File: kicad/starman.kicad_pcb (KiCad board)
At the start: 4 copper layers, 182 x 150 mm, 204 parts, among them J1 M20-8771246, J10 Barrel_Jack_MountingPin, J2 M20-8770646, J3 M20-8771246, J4 ESW-106-44-T-S, J5 Conn_02x03_Counter_Clockwise, J6 ESW-112-44-T-S, J7 Conn_01x10, J8 ESW-112-44-T-S, J9 Conn_01x10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

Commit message: DRC corrections
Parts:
- renumbered REF** to LOGO1, REF** to LOGO2
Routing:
- net Net-(D71-Pad1): track 32.7 -> 33.4 mm
- net Net-(D59-Pad1): track 22.0 -> 22.7 mm
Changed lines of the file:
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@@
     (descr "Open Source Hardware Logo")
     (tags "Logo OSHW")
-    (attr exclude_from_pos_files exclude_from_bom)
-    (fp_text reference "REF**" (at 0 0) (layer "F.SilkS") hide
+    (attr board_only exclude_from_pos_files exclude_from_bom)
+    (fp_text reference "LOGO2" (at 0 0) (layer "F.SilkS") hide
       (effects (font (size 1 1) (thickness 0.15)))
     )
@@
     (descr "KiCad Logo")
     (tags "Logo KiCad")
-    (attr exclude_from_pos_files exclude_from_bom)
-    (fp_text reference "REF**" (at 0 -5.08) (layer "F.SilkS") hide
+    (attr board_only exclude_from_pos_files exclude_from_bom)
+    (fp_text reference "LOGO1" (at 0 -5.08) (layer "F.SilkS") hide
       (effects (font (size 1 1) (thickness 0.15)))
     )
@@
   (segment (start 167.4625 89.7625) (end 175 97.3) (width 0.15) (layer "F.Cu") (net 16))
   (segment (start 152.5 89.7625) (end 167.4625 89.7625) (width 0.15) (layer "F.Cu") (net 16))
-  (segment (start 67.5 92.0125) (end 67.5 97.499022) (width 0.15) (layer "F.Cu") (net 17))
-  (segment (start 67.5 97.499022) (end 57.699022 107.3) (width 0.15) (layer "F.Cu") (net 17))
-  (segment (start 57.699022 107.3) (end 55 107.3) (width 0.15) (layer "F.Cu") (net 17))
+  (segment (start 67.5 92.0125) (end 67.5 98.7) (width 0.15) (layer "F.Cu") (net 17))
+  (segment (start 62.3 100) (end 55 107.3) (width 0.15) (layer "F.Cu") (net 17))
+  (segment (start 67.5 98.7) (end 66.2 100) (width 0.15) (layer "F.Cu") (net 17))
+  (segment (start 66.2 100) (end 62.3 100) (width 0.15) (layer "F.Cu") (net 17))
   (segment (start 68.2125 92.725) (end 68.2125 104.0875) (width 0.15) (layer "F.Cu") (net 18))
   (segment (start 68.2125 104.0875) (end 65 107.3) (width 0.15) (layer "F.Cu") (net 18))
@@
   (segment (start 70.2125 96.909644) (end 70.2125 92.725) (width 0.15) (layer "F.Cu") (net 20))
   (segment (start 73.402856 100.1) (end 70.2125 96.909644) (width 0.15) (layer "F.Cu") (net 20))
-  (segment (start 104.486072 119.5625) (end 103.25 118.326428) (width 0.15) (layer "F.Cu") (net 21))
-  (segment (start 103.25 118.326428) (end 103.25 109.05) (width 0.15) (layer "F.Cu") (net 21))
-  (segment (start 103.25 109.05) (end 105 107.3) (width 0.15) (layer "F.Cu") (net 21))
+  (segment (start 103.1 118.176428) (end 103.1 109.2) (width 0.15) (layer "F.Cu") (net 21))
+  (segment (start 104.486072 119.5625) (end 103.1 118.176428) (width 0.15) (layer "F.Cu") (net 21))
   (segment (start 107.5 119.5625) (end 104.486072 119.5625) (width 0.15) (layer "F.Cu") (net 21))
+  (segment (start 103.1 109.2) (end 105 107.3) (width 0.15) (layer "F.Cu") (net 21))
+  (segment (start 116.9 109.2) (end 115 107.3) (width 0.15) (layer "F.Cu") (net 22))
+  (segment (start 116.9 118.099022) (end 116.9 109.2) (width 0.15) (layer "F.Cu") (net 22))
+  (segment (start 115.436522 119.5625) (end 116.9 118.099022) (width 0.15) (layer "F.Cu") (net 22))
   (segment (start 112.525 119.5625) (end 115.436522 119.5625) (width 0.15) (layer "F.Cu") (net 22))
-  (segment (start 116.474511 118.524511) (end 116.474511 108.774511) (width 0.15) (layer "F.Cu") (net 22))
-  (segment (start 115.436522 119.5625) (end 116.474511 118.524511) (width 0.15) (layer "F.Cu") (net 22))
-  (segment (start 116.474511 108.774511) (end 115 107.3) (width 0.15) (layer "F.Cu") (net 22))
   (segment (start 146.724061 100.249511) (end 142.050489 100.249511) (width 0.15) (layer "F.Cu") (net 23))
   (segment (start 149.7875 97.186072) (end 146.724061 100.249511) (width 0.15) (layer "F.Cu") (net 23))
@@
   (segment (start 69.0125 111.3125) (end 75 117.3) (width 0.15) (layer "F.Cu") (net 28))
   (segment (start 69.0125 92.725) (end 69.0125 111.3125) (width 0.15) (layer "F.Cu") (net 28))
-  (segment (start 85 117.3) (end 82.227934 117.3) (width 0.15) (layer "F.Cu") (net 29))
-  (segment (start 69.4125 104.484566) (end 69.4125 92.725) (width 0.15) (layer "F.Cu") (net 29))
-  (segment (start 82.227934 117.3) (end 69.4125 104.484566) (width 0.15) (layer "F.Cu") (net 29))
+  (segment (start 77 109.7) (end 73.3 109.7) (width 0.15) (layer "F.Cu") (net 29))
+  (segment (start 73.3 109.7) (end 69.4125 105.8125) (width 0.15) (layer "F.Cu") (net 29))
+  (segment (start 69.4125 105.8125) (end 69.4125 92.725) (width 0.15) (layer "F.Cu") (net 29))
+  (segment (start 85 117.3) (end 84.6 117.3) (width 0.15) (layer "F.Cu") (net 29))
+  (segment (start 84.6 117.3) (end 77 109.7) (width 0.15) (layer "F.Cu") (net 29))
   (segment (start 100 119.3) (end 97 119.3) (width 0.15) (layer "F.Cu") (net 30))
   (segment (start 97 119.3) (end 95 117.3) (width 0.15) (layer "F.Cu") (net 30))
@@
   (segment (start 51.775 151.4) (end 48.025 155.15) (width 0.15) (layer "F.Cu") (net 161))
   (segment (start 38.075 174.225) (end 35 177.3) (width 0.15) (layer "F.Cu") (net 161))
-  (segment (start 38.075 165.125) (end 38.075 174.375) (width 0.15) (layer "F.Cu") (net 161))
   (segment (start 42.674999 160.375001) (end 38.075 164.975) (width 0.15) (layer "F.Cu") (net 161))
   (segment (start 48.025 155.15) (end 48.025 158.7) (width 0.15) (layer "F.Cu") (net 161))
@@
   (segment (start 46.349999 160.375001) (end 42.674999 160.375001) (width 0.15) (layer "F.Cu") (net 161))
   (segment (start 48.025 158.7) (end 46.349999 160.375001) (width 0.15) (layer "F.Cu") (net 161))
+  (segment (start 38.075 165) (end 38.075 174.375) (width 0.15) (layer "F.Cu") (net 161))
   (segment (start 51.64952 161.47548) (end 51.64952 170.65048) (width 0.15) (layer "F.Cu") (net 162))
   (segment (start 59.4 158.048572) (end 57.424061 160.024511) (width 0.15) (layer "F.Cu") (net 162))
@@
   (segment (start 133.4 90) (end 133.9 89.5) (width 0.15) (layer "F.Cu") (net 169))
   (segment (start 122.5 88.9375) (end 123.5625 90) (width 0.15) (layer "F.Cu") (net 169))
-  (segment (start 104.400489 98.700489) (end 104.9 99.2) (width 0.15) (layer "F.Cu") (net 169))
   (segment (start 159 147.4875) (end 158.951489 147.438989) (width 0.15) (layer "F.Cu") (net 169))
   (segment (start 146.768928 90.9625) (end 146.668439 90.862011) (width 0.15) (layer "F.Cu") (net 169))
@@
   (segment (start 120.7625 88.9375) (end 122.5 88.9375) (width 0.15) (layer "F.Cu") (net 169))
   (segment (start 143.862011 90.862011) (end 143.1 90.1) (width 0.15) (layer "F.Cu") (net 169))
-  (segment (start 102.2 95.9) (end 103.525489 97.225489) (width 0.15) (layer "F.Cu") (net 169))
   (segment (start 109.0125 117.65) (end 109.0125 113.4875) (width 0.15) (layer "F.Cu") (net 169))
   (segment (start 120.455216 85.702691) (end 121.447309 85.702691) (width 0.15) (layer "F.Cu") (net 169))
-  (segment (start 103.724061 98.700489) (end 104.400489 98.700489) (width 0.15) (layer "F.Cu") (net 169))
+  (segment (start 104.223572 99.2) (end 104.9 99.2) (width 0.15) (layer "F.Cu") (net 169))
   (segment (start 72.525 89.2125) (end 77.1125 89.2125) (width 0.15) (layer "F.Cu") (net 169))
   (segment (start 109.0125 113.4875) (end 109.2 113.3) (width 0.15) (layer "F.Cu") (net 169))
@@
   (segment (start 120.7625 88.9375) (end 119.477226 87.652226) (width 0.15) (layer "F.Cu") (net 169))
   (segment (start 59 143) (end 59.7 142.3) (width 0.15) (layer "F.Cu") (net 169))
-  (segment (start 102 95.9) (end 102.2 95.9) (width 0.15) (layer "F.Cu") (net 169))
   (segment (start 77.1125 89.2125) (end 77.4 89.5) (width 0.15) (layer "F.Cu") (net 169))
-  (segment (start 103.525489 98.501917) (end 103.724061 98.700489) (width 0.15) (layer "F.Cu") (net 169))
+  (segment (start 103.3 98.276428) (end 104.223572 99.2) (width 0.15) (layer "F.Cu") (net 169))
+  (segment (start 103.3 97) (end 103.3 98.276428) (width 0.15) (layer "F.Cu") (net 169))
   (segment (start 123.5625 90) (end 133.4 90) (width 0.15) (layer "F.Cu") (net 169))
   (segment (start 59 147.4875) (end 59 143) (width 0.15) (layer "F.Cu") (net 169))
-  (segment (start 103.525489 97.225489) (end 103.525489 98.501917) (width 0.15) (layer "F.Cu") (net 169))
+  (segment (start 102 95.9) (end 102.2 95.9) (width 0.15) (layer "F.Cu") (net 169))
+  (segment (start 102.2 95.9) (end 103.3 97) (width 0.15) (layer "F.Cu") (net 169))
   (segment (start 119.477226 87.652226) (end 119.477226 86.680681) (width 0.15) (layer "F.Cu") (net 169))
   (segment (start 147.475 90.9625) (end 146.768928 90.9625) (width 0.15) (layer "F.Cu") (net 169))

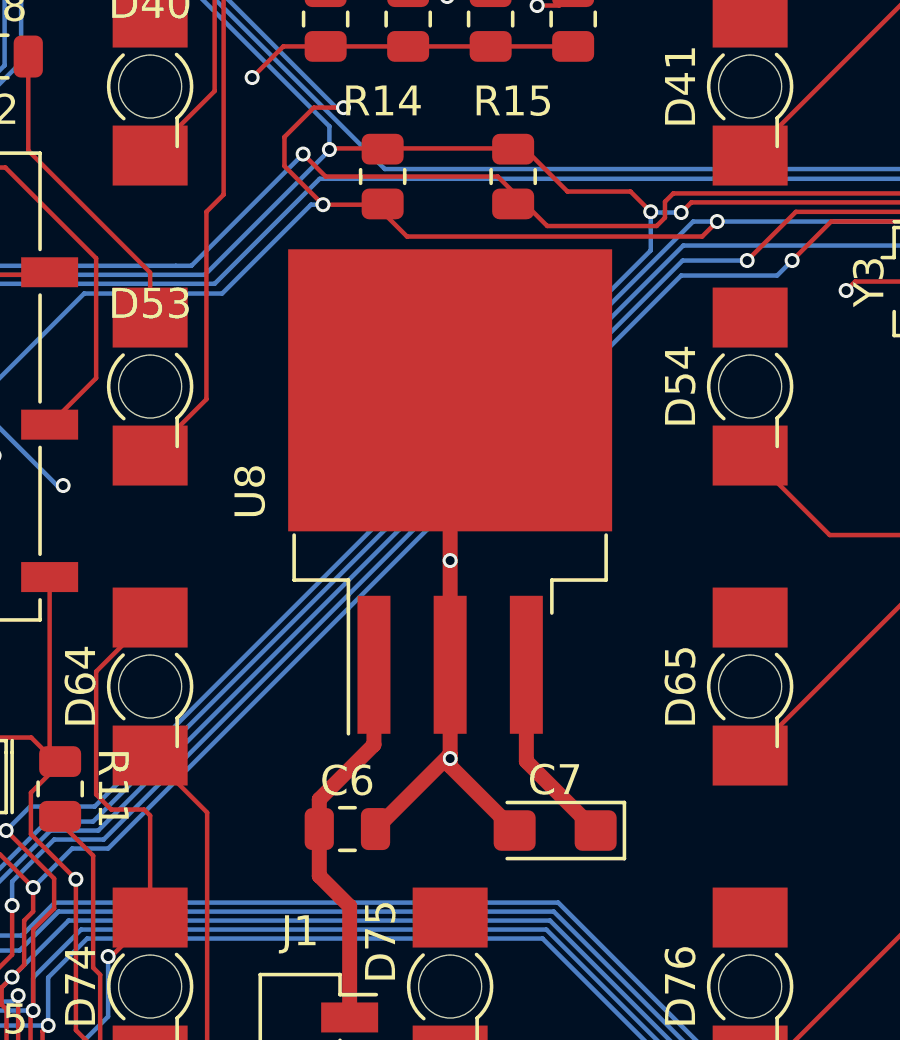
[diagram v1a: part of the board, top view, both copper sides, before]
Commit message: Updated part numbers for Y1..Y6, U8
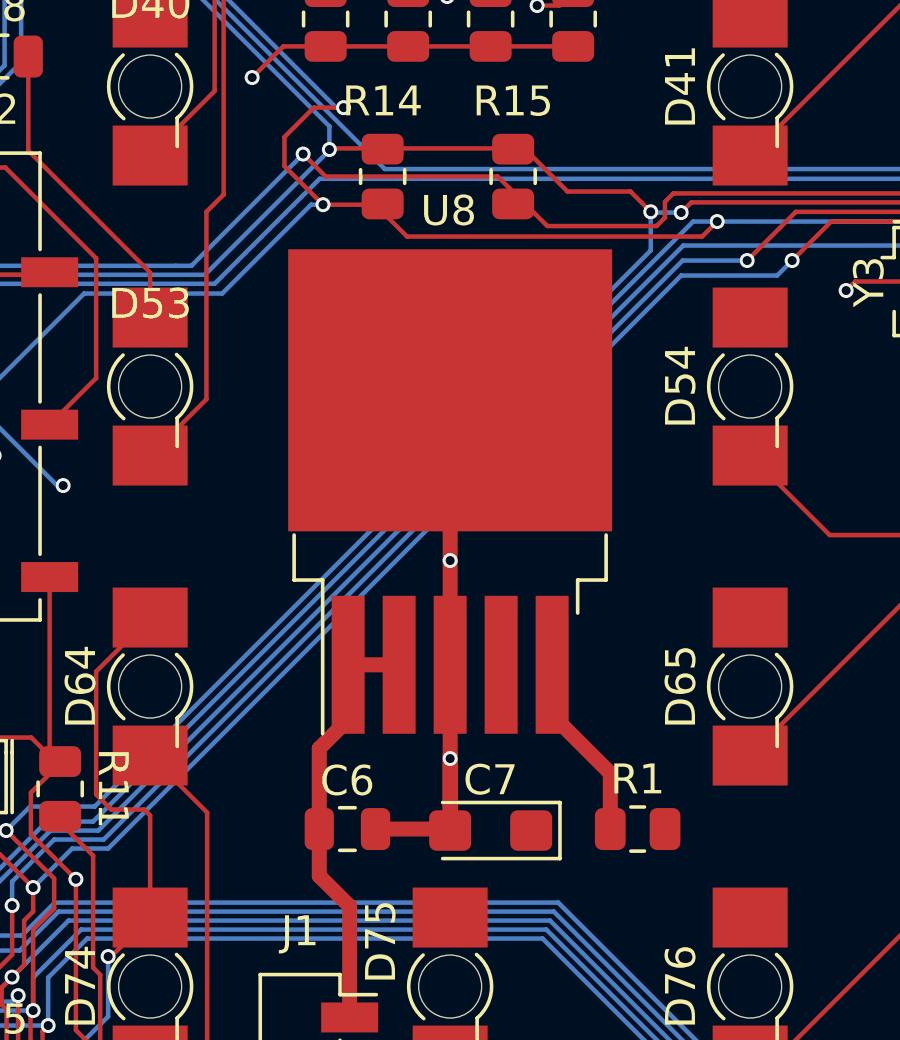
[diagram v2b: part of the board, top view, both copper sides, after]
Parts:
- added R1: 100k, Resistor_SMD:R_0805_2012Metric, F.Cu at (131.2, 109.8)
- C4, C6: value 0.1uF -> 1uF
- C7: value 10uF -> 47uF
- U8: value MIC29310-5.0WU -> NCP59300; footprint Package_TO_SOT_SMD:TO-263-3_TabPin2 -> Package_TO_SOT_SMD:TO-263-5_TabPin3
- moved C7 2.15 mm to (126.3, 109.8)
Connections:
- U8 pad 2: GND -> Net-(C6-Pad2)
- U8 pad 3: +5V -> GND
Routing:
- net Net-(U8-Pad5): track 0.00 -> 8.05 mm
- net +5V: track 251.9 -> 245.4 mm
- net Net-(C6-Pad2): track 12.9 -> 14.3 mm
- net GND: track 225.7 -> 226.3 mm

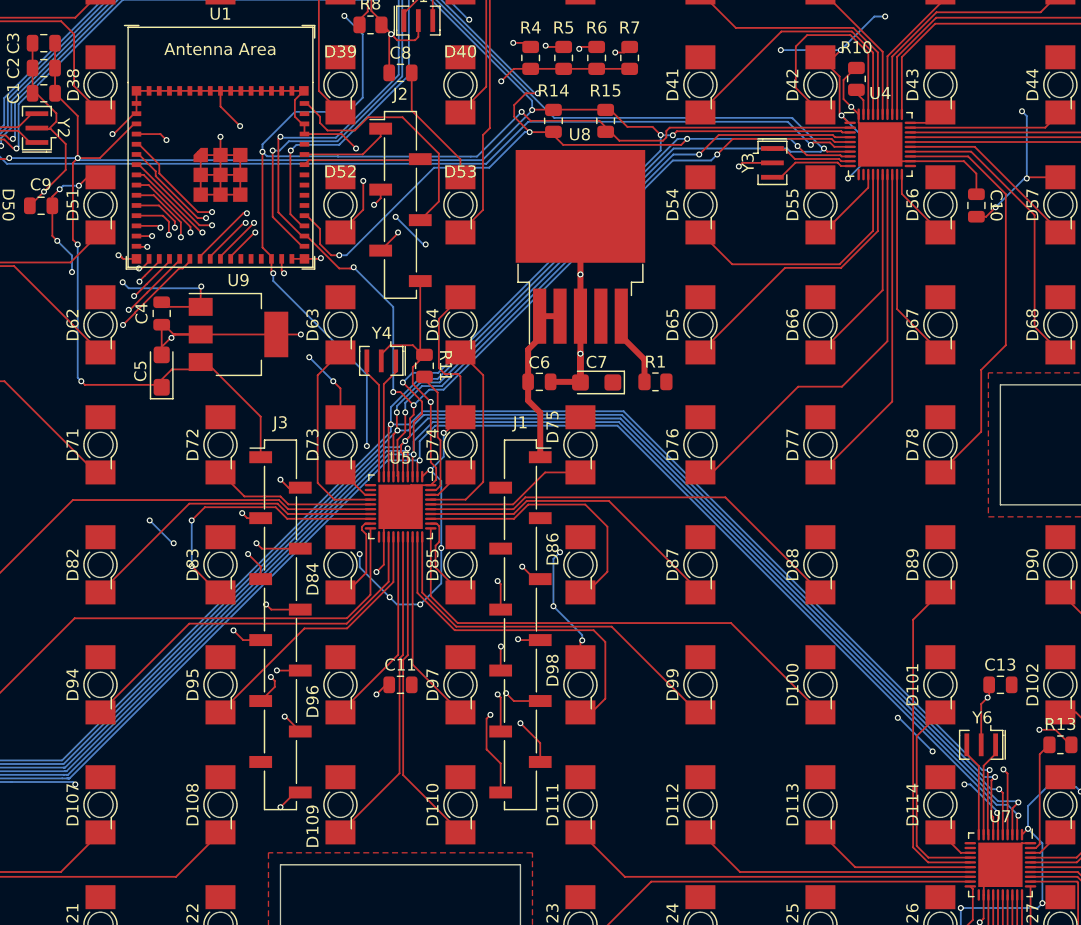
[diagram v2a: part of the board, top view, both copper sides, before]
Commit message: Minor adjustments to align with stock available.
- Adjusted J1 and J3 to be SMD headers (pin right)
- Adjusted J6 and J7 to be sockets,
- Restored R1 as part of U8
- U9 is actually TO-252-3
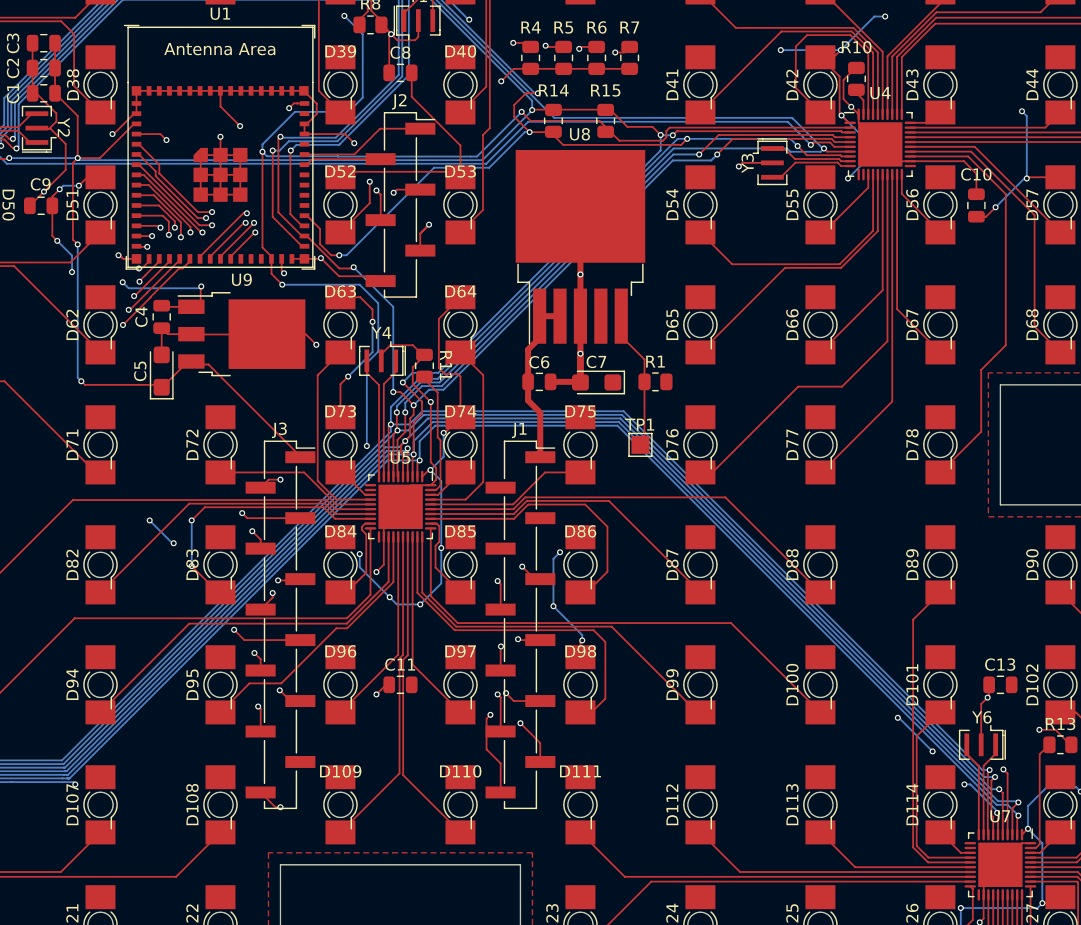
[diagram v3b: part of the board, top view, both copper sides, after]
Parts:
- added TP1: TestPoint, TestPoint:TestPoint_Pad_1.5x1.5mm, F.Cu at (130.0, 115.0)
- J1: footprint Connector_PinSocket_2.54mm:PinSocket_1x12_P2.54mm_Vertical_SMD_Pin1Right -> Connector_PinHeader_2.54mm:PinHeader_1x12_P2.54mm_Vertical_SMD_Pin1Right
- J2: value M20-8770646 -> M20-8771246; footprint Connector_PinSocket_2.54mm:PinSocket_1x06_P2.54mm_Vertical_SMD_Pin1Left -> Connector_PinHeader_2.54mm:PinHeader_1x06_P2.54mm_Vertical_SMD_Pin1Right
- J3: footprint Connector_PinSocket_2.54mm:PinSocket_1x12_P2.54mm_Vertical_SMD_Pin1Left -> Connector_PinHeader_2.54mm:PinHeader_1x12_P2.54mm_Vertical_SMD_Pin1Right
- J4: footprint Connector_PinHeader_2.54mm:PinHeader_1x06_P2.54mm_Vertical -> Connector_PinSocket_2.54mm:PinSocket_1x06_P2.54mm_Vertical
- J6, J8: footprint Connector_PinHeader_2.54mm:PinHeader_1x12_P2.54mm_Vertical -> Connector_PinSocket_2.54mm:PinSocket_1x12_P2.54mm_Vertical
- U8: value NCP59300 -> NCP59301
- U9: value LF33_TO220 -> LF33; footprint Package_TO_SOT_SMD:SOT-223-3_TabPin2 -> Package_TO_SOT_SMD:TO-252-3_TabPin2
- moved C4 0.29 mm to (90.1, 104.3)
- moved U9 0.28 mm to (96.8, 105.8)
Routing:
- net /GPIO6: track 58.1 -> 120.3 mm, vias 2 -> 4
- net /GPIO8: track 62.2 -> 0.00 mm, vias 2 -> 0
- net +5V: track 245.4 -> 259.4 mm, vias 52 -> 50
- net /EN: track 20.3 -> 14.3 mm, vias 0 -> 2
- net Net-(R1-Pad1): track 8.05 -> 13.4 mm
- net /RESET: track 289.1 -> 293.7 mm
- net /GPIO9: track 30.5 -> 33.8 mm
- net /GPIO13: track 37.7 -> 41.0 mm
- net /TXD: track 9.84 -> 6.54 mm
- net /GPIO10: track 34.3 -> 31.1 mm
- net GND: track 226.3 -> 223.1 mm, vias 29 -> 28
- net /RXD: track 7.62 -> 10.5 mm
- net /GPIO11: track 32.5 -> 35.3 mm
- net /GPIO14: track 43.1 -> 40.3 mm
- net /GPIO0: track 24.0 -> 26.4 mm
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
